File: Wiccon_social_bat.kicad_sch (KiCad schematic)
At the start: 19 parts, among them J1 SAO, SW1 Change, U1 CH32V003

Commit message: Small changes to art, changed sw1
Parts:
- SW1: footprint Button_Switch_SMD:SW_SPST_B3SL-1002P -> Button_Switch_SMD:SW_Push_1P1T_XKB_TS-1187A; LCSC ??? -> C318884
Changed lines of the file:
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@@
 			)
 		)
-		(property "Footprint" "Button_Switch_SMD:SW_SPST_B3SL-1002P"
+		(property "Footprint" "Button_Switch_SMD:SW_Push_1P1T_XKB_TS-1187A"
 			(at 114.3 106.68 0)
 			(effects
@@
 			)
 		)
-		(property "LCSC" "???"
+		(property "LCSC" "C318884"
 			(at 114.3 111.76 0)
 			(effects
@@
 		)
 		(instances
-			(project ""
+			(project "Wiccon_social_bat"
 				(path "/575bcede-8866-4ca7-a1ba-9804eb5c9e06"
 					(reference "#PWR01")
@@
 		)
 		(instances
-			(project ""
+			(project "Wiccon_social_bat"
 				(path "/575bcede-8866-4ca7-a1ba-9804eb5c9e06"
 					(reference "N2")
@@
 		)
 		(instances
-			(project ""
+			(project "Wiccon_social_bat"
 				(path "/575bcede-8866-4ca7-a1ba-9804eb5c9e06"
 					(reference "N1")
@@
 		)
 		(instances
-			(project ""
+			(project "Wiccon_social_bat"
 				(path "/575bcede-8866-4ca7-a1ba-9804eb5c9e06"
 					(reference "R1")

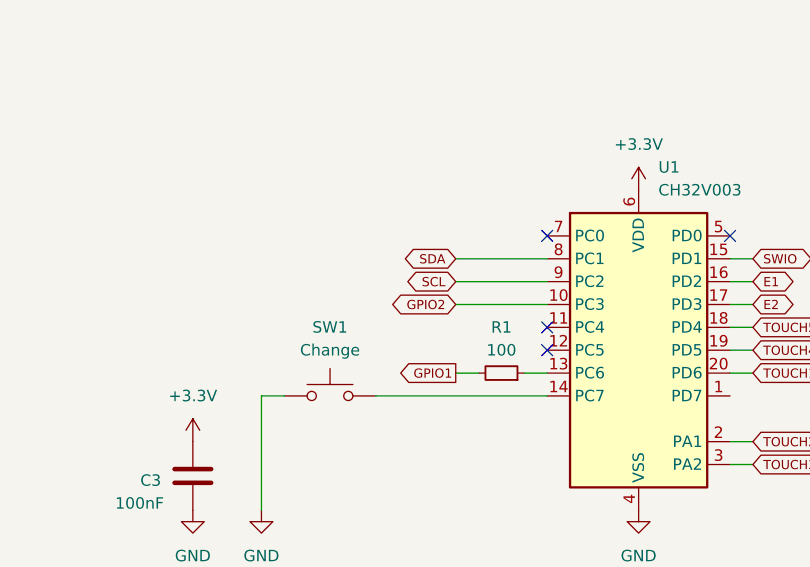
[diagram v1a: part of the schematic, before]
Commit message: Move WICCON.NL text
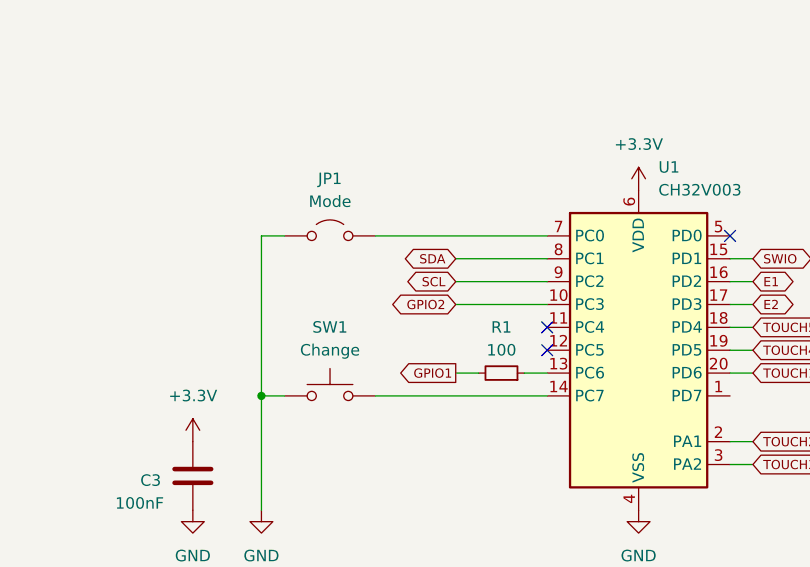
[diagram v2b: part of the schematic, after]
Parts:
- added JP1: Mode, Jumper:SolderJumper-2_P1.3mm_Open_RoundedPad1.0x1.5mm, symbol Jumper:Jumper_2_Open
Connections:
- net GND: now also JP1.1 (A)
- net at U1.7 (PC0): now also JP1.2 (B)
- no-connect marks 5 -> 4
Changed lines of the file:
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@@
 	(generator_version "8.0")
 	(paper "A4")
+	(junction
+		(at 106.68 111.76)
+		(diameter 0)
+		(color 0 0 0 0)
+	)
 	(no_connect
 		(at 138.43 104.14)
 	)
 	(no_connect
-		(at 138.43 93.98)
-	)
-	(no_connect
 		(at 158.75 93.98)
 	)
@@
 	(wire
 		(pts
+			(xy 106.68 93.98) (xy 109.22 93.98)
+		)
+		(stroke
+			(width 0)
+			(type default)
+		)
+	)
+	(wire
+		(pts
 			(xy 161.29 119.38) (xy 158.75 119.38)
 		)
@@
 	(wire
 		(pts
+			(xy 106.68 93.98) (xy 106.68 111.76)
+		)
+		(stroke
+			(width 0)
+			(type default)
+		)
+	)
+	(wire
+		(pts
 			(xy 119.38 111.76) (xy 138.43 111.76)
 		)
@@
 		(pts
 			(xy 243.84 36.83) (xy 248.92 36.83)
+		)
+		(stroke
+			(width 0)
+			(type default)
+		)
+	)
+	(wire
+		(pts
+			(xy 119.38 93.98) (xy 138.43 93.98)
 		)
 		(stroke
@@
 					(unit 1)
 				)
+			)
+		)
+	)
+	(symbol
+		(lib_id "Jumper:Jumper_2_Open")
+		(at 114.3 93.98 0)
+		(unit 1)
+		(exclude_from_sim yes)
+		(in_bom no)
+		(on_board yes)
+		(dnp no)
+		(fields_autoplaced yes)
+		(property "Reference" "JP1"
+			(at 114.3 87.63 0)
+			(effects
+				(font
+					(size 1.27 1.27)
+				)
+			)
+		)
+		(property "Value" "Mode"
+			(at 114.3 90.17 0)
+			(effects
+				(font
+					(size 1.27 1.27)
+				)
+			)
+		)
+		(property "Footprint" "Jumper:SolderJumper-2_P1.3mm_Open_RoundedPad1.0x1.5mm"
+			(at 114.3 93.98 0)
+			(effects
+				(font
+					(size 1.27 1.27)
+				)
+				(hide yes)
+			)
+		)
+		(property "Datasheet" ""
+			(at 114.3 93.98 0)
+			(effects
+				(font
+					(size 1.27 1.27)
+				)
+				(hide yes)
+			)
+		)
+		(property "Description" ""
+			(at 114.3 93.98 0)
+			(effects
+				(font
+					(size 1.27 1.27)
+				)
+				(hide yes)
+			)
+		)
+		(pin "1"
+		)
+		(pin "2"
+		)
+		(instances
+			(project ""
+				(path "/575bcede-8866-4ca7-a1ba-9804eb5c9e06"
+					(reference "JP1")
+					(unit 1)
+				)
